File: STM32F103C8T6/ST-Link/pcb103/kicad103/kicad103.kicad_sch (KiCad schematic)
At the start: 16 parts, among them IC1 LD1117DT33TR, J1 0480372200, J2 Conn_01x02_Socket, U1 STM32F103C8T6

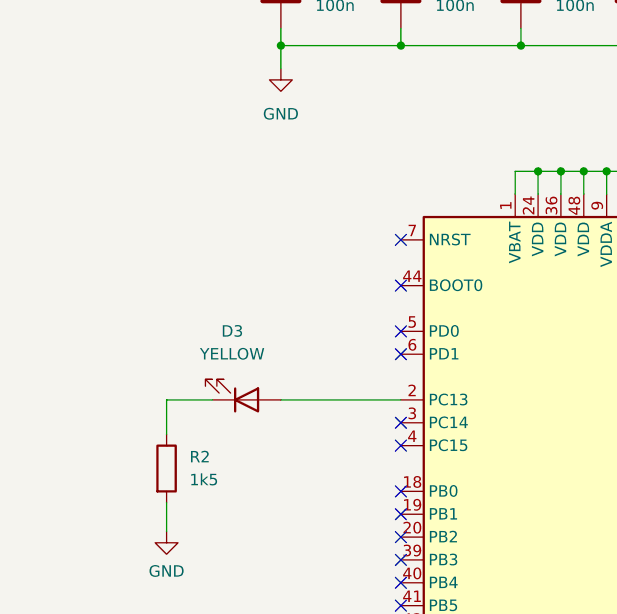
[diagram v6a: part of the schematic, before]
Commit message: Add 8MHz crystal
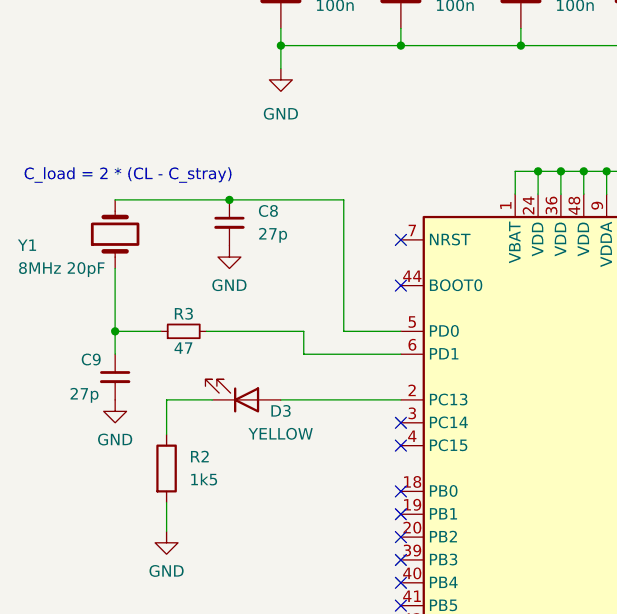
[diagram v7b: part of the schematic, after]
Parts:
- added C8, C9: 27p, Capacitor_SMD:C_0402_1005Metric, symbol Device:C_Small
- added R3: 47, Resistor_SMD:R_0402_1005Metric, symbol Device:R_Small
- added Y1: 8MHz 20pF, Crystal:Crystal_SMD_5032-2Pin_5.0x3.2mm, symbol Device:Crystal
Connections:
- net GND: now also C8.2, C9.2
- net at U1.5 (PD0): now also C8.1, Y1.2
- net at U1.6 (PD1): now also R3.2
- new net: C9.1, R3.1, Y1.1
- no-connect marks 40 -> 38
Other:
- note added: "C_load = 2 * (CL - C_stray)"
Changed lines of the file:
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@@
   (junction (at 107.95 55.88) (diameter 0) (color 0 0 0 0)
   )
+  (junction (at 37.465 100.33) (diameter 0) (color 0 0 0 0)
+  )
   (junction (at 95.25 55.88) (diameter 0) (color 0 0 0 0)
   )
@@
   )
   (junction (at 196.85 28.575) (diameter 0) (color 0 0 0 0)
+  )
+  (junction (at 50.165 85.725) (diameter 0) (color 0 0 0 0)
   )
   (junction (at 208.915 42.545) (diameter 0) (color 0 0 0 0)
@@
   (no_connect (at 69.215 133.35))
   (no_connect (at 69.215 90.17))
-  (no_connect (at 69.215 102.87))
   (no_connect (at 102.235 125.73))
   (no_connect (at 69.215 110.49))
@@
   (no_connect (at 69.215 143.51))
   (no_connect (at 102.235 100.33))
-  (no_connect (at 69.215 100.33))
   (no_connect (at 102.235 90.17))
   (no_connect (at 69.215 130.81))
@@
     (stroke (width 0) (type default))
   )
+  (wire (pts (xy 58.42 100.33) (xy 47.625 100.33))
+    (stroke (width 0) (type default))
+  )
   (wire (pts (xy 95.25 55.88) (xy 107.95 55.88))
     (stroke (width 0) (type default))
@@
     (stroke (width 0) (type default))
   )
+  (wire (pts (xy 37.465 93.345) (xy 37.465 100.33))
+    (stroke (width 0) (type default))
+  )
   (wire (pts (xy 107.95 55.88) (xy 107.95 59.055))
     (stroke (width 0) (type default))
@@
     (stroke (width 0) (type default))
   )
+  (wire (pts (xy 37.465 100.33) (xy 37.465 102.87))
+    (stroke (width 0) (type default))
+  )
   (wire (pts (xy 150.495 33.655) (xy 150.495 120.65))
     (stroke (width 0) (type default))
@@
     (stroke (width 0) (type default))
   )
+  (wire (pts (xy 62.865 85.725) (xy 62.865 100.33))
+    (stroke (width 0) (type default))
+  )
   (wire (pts (xy 69.215 55.88) (xy 82.55 55.88))
     (stroke (width 0) (type default))
@@
     (stroke (width 0) (type default))
   )
+  (wire (pts (xy 50.165 85.725) (xy 37.465 85.725))
+    (stroke (width 0) (type default))
+  )
+  (wire (pts (xy 69.215 100.33) (xy 62.865 100.33))
+    (stroke (width 0) (type default))
+  )
   (wire (pts (xy 82.55 55.88) (xy 95.25 55.88))
     (stroke (width 0) (type default))
@@
     (stroke (width 0) (type default))
   )
+  (wire (pts (xy 58.42 102.87) (xy 69.215 102.87))
+    (stroke (width 0) (type default))
+  )
   (wire (pts (xy 164.465 28.575) (xy 182.88 28.575))
     (stroke (width 0) (type default))
@@
     (stroke (width 0) (type default))
   )
+  (wire (pts (xy 37.465 100.33) (xy 42.545 100.33))
+    (stroke (width 0) (type default))
+  )
   (wire (pts (xy 158.75 41.275) (xy 158.75 45.085))
     (stroke (width 0) (type default))
@@
     (stroke (width 0) (type default))
   )
+  (wire (pts (xy 62.865 85.725) (xy 50.165 85.725))
+    (stroke (width 0) (type default))
+  )
+  (wire (pts (xy 58.42 102.87) (xy 58.42 100.33))
+    (stroke (width 0) (type default))
+  )
   (wire (pts (xy 86.995 82.55) (xy 86.995 85.09))
     (stroke (width 0) (type default))
@@
   (wire (pts (xy 116.84 55.88) (xy 121.92 55.88))
     (stroke (width 0) (type default))
+  )
+  (text "C_load = 2 * (CL - C_stray)" (at 27.305 83.82 0)
+    (effects (font (size 1.27 1.27)) (justify left bottom))
   )
   (label "USB_D-" (at 109.855 118.11 0) (fields_autoplaced)
@@
         (path "/185c057b-9149-49f2-8708-a9b3e40a18db"
           (reference "#PWR02") (unit 1)
+        )
+      )
+    )
+  )
+  (symbol (lib_id "Device:R_Small") (at 45.085 100.33 90) (unit 1)
+    (in_bom yes) (on_board yes) (dnp no)
+    (property "Reference" "R3" (at 45.085 98.425 90)
+      (effects (font (size 1.27 1.27)))
+    )
+    (property "Value" "47" (at 45.085 102.235 90)
+      (effects (font (size 1.27 1.27)))
+    )
+    (property "Footprint" "Resistor_SMD:R_0402_1005Metric" (at 45.085 100.33 0)
+      (effects (font (size 1.27 1.27)) hide)
+    )
+    (property "Datasheet" "~" (at 45.085 100.33 0)
+      (effects (font (size 1.27 1.27)) hide)
+    )
+    (pin "1")
+    (pin "2")
+    (instances
+      (project "kicad103"
+        (path "/185c057b-9149-49f2-8708-a9b3e40a18db"
+          (reference "R3") (unit 1)
+        )
+      )
+    )
+  )
+  (symbol (lib_id "Device:C_Small") (at 50.165 88.265 0) (unit 1)
+    (in_bom yes) (on_board yes) (dnp no) (fields_autoplaced)
+    (property "Reference" "C8" (at 53.34 87.0013 0)
+      (effects (font (size 1.27 1.27)) (justify left))
+    )
+    (property "Value" "27p" (at 53.34 89.5413 0)
+      (effects (font (size 1.27 1.27)) (justify left))
+    )
+    (property "Footprint" "Capacitor_SMD:C_0402_1005Metric" (at 50.165 88.265 0)
+      (effects (font (size 1.27 1.27)) hide)
+    )
+    (property "Datasheet" "~" (at 50.165 88.265 0)
+      (effects (font (size 1.27 1.27)) hide)
+    )
+    (pin "1")
+    (pin "2")
+    (instances
+      (project "kicad103"
+        (path "/185c057b-9149-49f2-8708-a9b3e40a18db"
+          (reference "C8") (unit 1)
         )
       )
@@
     )
   )
+  (symbol (lib_id "Device:C_Small") (at 37.465 105.41 0) (unit 1)
+    (in_bom yes) (on_board yes) (dnp no)
+    (property "Reference" "C9" (at 33.655 103.505 0)
+      (effects (font (size 1.27 1.27)) (justify left))
+    )
+    (property "Value" "27p" (at 32.385 107.315 0)
+      (effects (font (size 1.27 1.27)) (justify left))
+    )
+    (property "Footprint" "Capacitor_SMD:C_0402_1005Metric" (at 37.465 105.41 0)
+      (effects (font (size 1.27 1.27)) hide)
+    )
+    (property "Datasheet" "~" (at 37.465 105.41 0)
+      (effects (font (size 1.27 1.27)) hide)
+    )
+    (pin "1")
+    (pin "2")
+    (instances
+      (project "kicad103"
+        (path "/185c057b-9149-49f2-8708-a9b3e40a18db"
+          (reference "C9") (unit 1)
+        )
+      )
+    )
+  )
   (symbol (lib_id "power:GND") (at 252.095 49.53 0) (unit 1)
     (in_bom yes) (on_board yes) (dnp no) (fields_autoplaced)
@@
   (symbol (lib_id "Device:LED") (at 52.07 107.95 0) (mirror x) (unit 1)
     (in_bom yes) (on_board yes) (dnp no)
-    (property "Reference" "D3" (at 50.4825 100.33 0)
-      (effects (font (size 1.27 1.27)))
-    )
-    (property "Value" "YELLOW" (at 50.4825 102.87 0)
+    (property "Reference" "D3" (at 55.88 109.22 0)
+      (effects (font (size 1.27 1.27)))
+    )
+    (property "Value" "YELLOW" (at 55.88 111.76 0)
       (effects (font (size 1.27 1.27)))
     )
@@
         (path "/185c057b-9149-49f2-8708-a9b3e40a18db"
           (reference "D2") (unit 1)
+        )
+      )
+    )
+  )
+  (symbol (lib_id "Device:Crystal") (at 37.465 89.535 90) (unit 1)
+    (in_bom yes) (on_board yes) (dnp no)
+    (property "Reference" "Y1" (at 26.67 90.805 90)
+      (effects (font (size 1.27 1.27)) (justify right))
+    )
+    (property "Value" "8MHz 20pF" (at 26.67 93.345 90)
+      (effects (font (size 1.27 1.27)) (justify right))
+    )
+    (property "Footprint" "Crystal:Crystal_SMD_5032-2Pin_5.0x3.2mm" (at 37.465 89.535 0)
+      (effects (font (size 1.27 1.27)) hide)
+    )
+    (property "Datasheet" "~" (at 37.465 89.535 0)
+      (effects (font (size 1.27 1.27)) hide)
+    )
+    (pin "1")
+    (pin "2")
+    (instances
+      (project "kicad103"
+        (path "/185c057b-9149-49f2-8708-a9b3e40a18db"
+          (reference "Y1") (unit 1)
         )
       )
@@
     )
   )
+  (symbol (lib_id "power:GND") (at 37.465 107.95 0) (unit 1)
+    (in_bom yes) (on_board yes) (dnp no) (fields_autoplaced)
+    (property "Reference" "#PWR011" (at 37.465 114.3 0)
+      (effects (font (size 1.27 1.27)) hide)
+    )
+    (property "Value" "GND" (at 37.465 112.395 0)
+      (effects (font (size 1.27 1.27)))
+    )
+    (property "Footprint" "" (at 37.465 107.95 0)
+      (effects (font (size 1.27 1.27)) hide)
+    )
+    (property "Datasheet" "" (at 37.465 107.95 0)
+      (effects (font (size 1.27 1.27)) hide)
+    )
+    (pin "1")
+    (instances
+      (project "kicad103"
+        (path "/185c057b-9149-49f2-8708-a9b3e40a18db"
+          (reference "#PWR011") (unit 1)
+        )
+      )
+    )
+  )
   (symbol (lib_id "New_Library:0480372200") (at 113.03 36.195 0) (mirror x) (unit 1)
     (in_bom yes) (on_board yes) (dnp no)
@@
         )
       )
+    )
+  )
+  (symbol (lib_id "power:GND") (at 50.165 90.805 0) (unit 1)
+    (in_bom yes) (on_board yes) (dnp no) (fields_autoplaced)
+    (property "Reference" "#PWR010" (at 50.165 97.155 0)
+      (effects (font (size 1.27 1.27)) hide)
+    )
+    (property "Value" "GND" (at 50.165 95.25 0)
+      (effects (font (size 1.27 1.27)))
+    )
+    (property "Footprint" "" (at 50.165 90.805 0)
+      (effects (font (size 1.27 1.27)) hide)
+    )
+    (property "Datasheet" "" (at 50.165 90.805 0)
+      (effects (font (size 1.27 1.27)) hide)
+    )
+    (pin "1")
+    (instances
+      (project "kicad103"
+        (path "/185c057b-9149-49f2-8708-a9b3e40a18db"
+          (reference "#PWR010") (unit 1)
+        )
+      )

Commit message: Pull-up resistor on USB_DP line
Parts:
- added R4: 1k5, Resistor_SMD:R_0805_2012Metric, symbol Device:R
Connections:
- net USB_D+: now also R4.2
- net +3.3V: now reaches C3.1, C4.1, C5.1, C6.1, C7.1, U1.1 (VBAT), U1.24 (VDD), U1.36 (VDD), U1.48 (VDD), U1.9 (VDDA)
- net +3.3V: now also R4.1
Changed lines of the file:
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@@
   (junction (at 196.85 42.545) (diameter 0) (color 0 0 0 0)
   )
+  (junction (at 55.88 55.88) (diameter 0) (color 0 0 0 0)
+  )
   (junction (at 69.215 68.58) (diameter 0) (color 0 0 0 0)
   )
@@
   )
   (junction (at 208.915 42.545) (diameter 0) (color 0 0 0 0)
+  )
+  (junction (at 131.445 120.65) (diameter 0) (color 0 0 0 0)
   )
   (junction (at 84.455 82.55) (diameter 0) (color 0 0 0 0)
@@
     (stroke (width 0) (type default))
   )
+  (wire (pts (xy 131.445 104.14) (xy 131.445 106.68))
+    (stroke (width 0) (type default))
+  )
+  (wire (pts (xy 131.445 114.3) (xy 131.445 120.65))
+    (stroke (width 0) (type default))
+  )
   (wire (pts (xy 208.915 42.545) (xy 208.915 46.99))
     (stroke (width 0) (type default))
@@
     (stroke (width 0) (type default))
   )
-  (wire (pts (xy 150.495 120.65) (xy 102.235 120.65))
+  (wire (pts (xy 150.495 120.65) (xy 131.445 120.65))
     (stroke (width 0) (type default))
   )
@@
   )
   (wire (pts (xy 58.42 102.87) (xy 58.42 100.33))
+    (stroke (width 0) (type default))
+  )
+  (wire (pts (xy 131.445 120.65) (xy 102.235 120.65))
     (stroke (width 0) (type default))
   )
@@
         (path "/185c057b-9149-49f2-8708-a9b3e40a18db"
           (reference "#PWR04") (unit 1)
+        )
+      )
+    )
+  )
+  (symbol (lib_id "Device:R") (at 131.445 110.49 0) (unit 1)
+    (in_bom yes) (on_board yes) (dnp no) (fields_autoplaced)
+    (property "Reference" "R4" (at 133.985 109.22 0)
+      (effects (font (size 1.27 1.27)) (justify left))
+    )
+    (property "Value" "1k5" (at 133.985 111.76 0)
+      (effects (font (size 1.27 1.27)) (justify left))
+    )
+    (property "Footprint" "Resistor_SMD:R_0805_2012Metric" (at 129.667 110.49 90)
+      (effects (font (size 1.27 1.27)) hide)
+    )
+    (property "Datasheet" "~" (at 131.445 110.49 0)
+      (effects (font (size 1.27 1.27)) hide)
+    )
+    (pin "1")
+    (pin "2")
+    (instances
+      (project "kicad103"
+        (path "/185c057b-9149-49f2-8708-a9b3e40a18db"
+          (reference "R4") (unit 1)
         )
       )
@@
         )
       )
+    )
+  )
+  (symbol (lib_id "power:+3.3V") (at 55.88 55.88 0) (unit 1)
+    (in_bom yes) (on_board yes) (dnp no) (fields_autoplaced)
+    (property "Reference" "#PWR012" (at 55.88 59.69 0)
+      (effects (font (size 1.27 1.27)) hide)
+    )
+    (property "Value" "+3.3V" (at 55.88 50.8 0)
+      (effects (font (size 1.27 1.27)))
+    )
+    (property "Footprint" "" (at 55.88 55.88 0)
+      (effects (font (size 1.27 1.27)) hide)
+    )
+    (property "Datasheet" "" (at 55.88 55.88 0)
+      (effects (font (size 1.27 1.27)) hide)
+    )
+    (pin "1")
+    (instances
+      (project "kicad103"
+        (path "/185c057b-9149-49f2-8708-a9b3e40a18db"
+          (reference "#PWR012") (unit 1)
+        )
+      )
+    )
+  )
+  (symbol (lib_id "power:+3.3V") (at 131.445 104.14 0) (unit 1)
+    (in_bom yes) (on_board yes) (dnp no) (fields_autoplaced)
+    (property "Reference" "#PWR013" (at 131.445 107.95 0)
+      (effects (font (size 1.27 1.27)) hide)
+    )
+    (property "Value" "+3.3V" (at 131.445 99.06 0)
+      (effects (font (size 1.27 1.27)))
+    )
+    (property "Footprint" "" (at 131.445 104.14 0)
+      (effects (font (size 1.27 1.27)) hide)
+    )
+    (property "Datasheet" "" (at 131.445 104.14 0)
+      (effects (font (size 1.27 1.27)) hide)
+    )
+    (pin "1")
+    (instances
+      (project "kicad103"
+        (path "/185c057b-9149-49f2-8708-a9b3e40a18db"
+          (reference "#PWR013") (unit 1)
+        )
+      )
